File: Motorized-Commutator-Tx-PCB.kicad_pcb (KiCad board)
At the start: 2 copper layers, 100 x 50 mm, 18 parts, among them J1 NRF24L01, J2 Conn_01x10_Female, J3 Conn_01x14_Female, U1 LEFT_STICK, U2 Teensy4.0, U3 LD1117S33TR_SOT223, U4 RIGHT_STICK

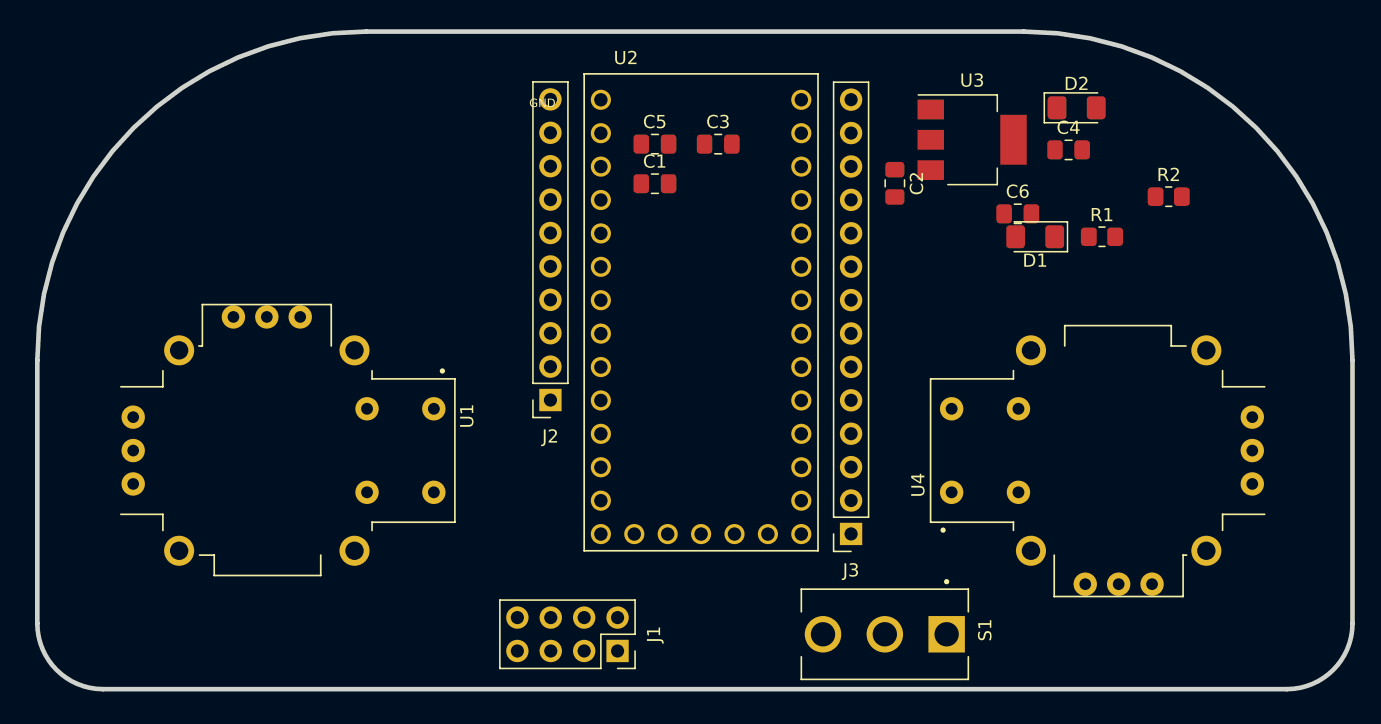
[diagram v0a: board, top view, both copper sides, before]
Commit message: Rewired some connections and completed PCB connections
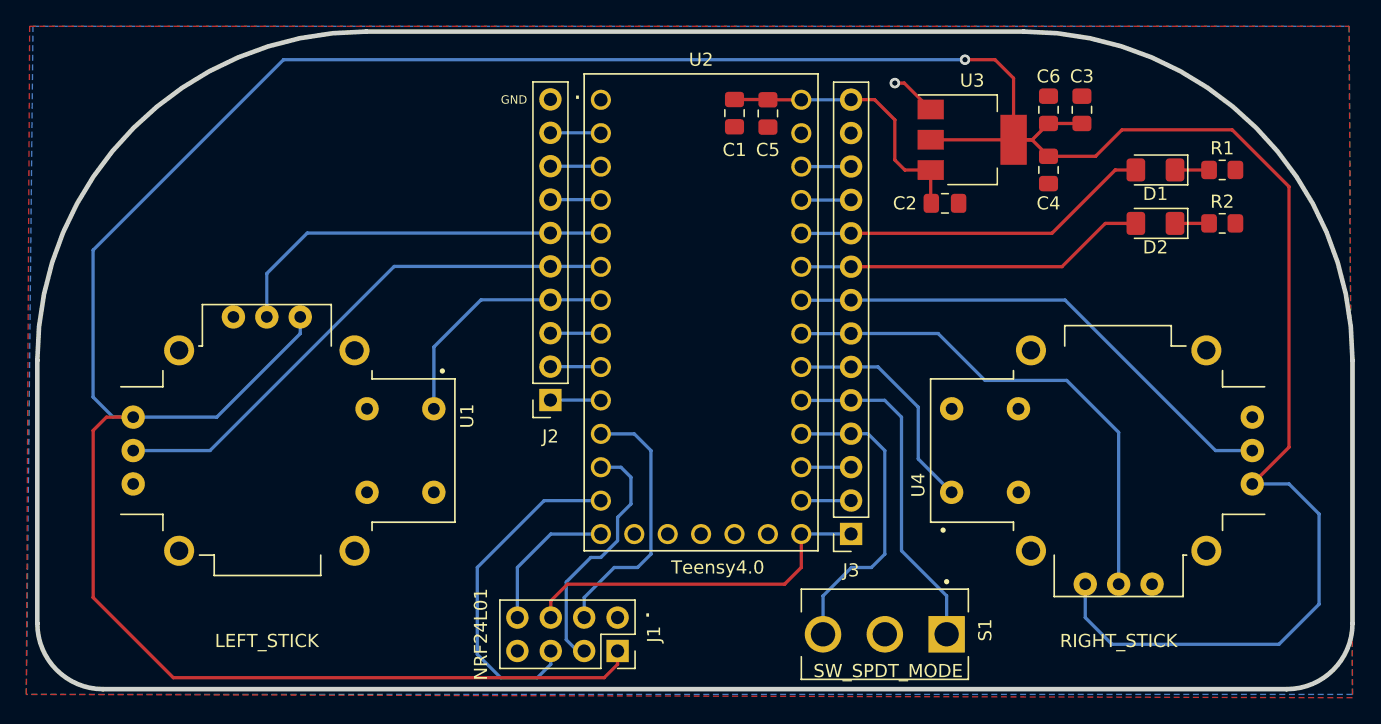
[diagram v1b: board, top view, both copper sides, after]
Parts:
- moved C3 27.8 mm to (156.0, 106.2), turned to 90 degrees
- moved D2 10.6 mm to (161.5, 114.8), turned to 180 degrees
- moved D1 10.5 mm to (161.5, 110.7)
- moved R1 10.5 mm to (166.6, 110.7)
- moved C5 8.90 mm to (132.1, 106.4), turned to -90 degrees
- moved C6 8.25 mm to (153.4, 106.2), turned to 90 degrees
- moved C1 8.09 mm to (129.5, 106.4), turned to -90 degrees
- moved R2 4.54 mm to (166.6, 114.8)
- moved C2 4.10 mm to (145.5, 113.3), turned to 0 degrees
- moved C4 2.16 mm to (153.4, 110.7), turned to -90 degrees
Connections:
- J3 pad 10: Net-(J3-Pad10) -> MANUAL
- J3 pad 2: AUTO -> Net-(J3-Pad2)
- J3 pad 3: MANUAL -> Net-(J3-Pad3)
- J3 pad 6: RIGHT_V -> RIGHT_B
- J3 pad 7: RIGHT_H -> RIGHT_V
- J3 pad 8: RIGHT_B -> RIGHT_H
- J3 pad 9: Net-(J3-Pad9) -> AUTO
- U2 pad 14: AUTO -> Net-(J3-Pad2)
- U2 pad 15: MANUAL -> Net-(J3-Pad3)
- U2 pad 18: RIGHT_V -> RIGHT_B
- U2 pad 19: RIGHT_H -> RIGHT_V
- U2 pad 20: RIGHT_B -> RIGHT_H
- U2 pad 21: Net-(J3-Pad9) -> AUTO
- U2 pad 22: Net-(J3-Pad10) -> MANUAL
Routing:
- net 3.3V: track 0.00 -> 267.9 mm, vias 0 -> 1
- net LEFT_H: track 0.00 -> 41.4 mm
- net RIGHT_H: track 0.00 -> 39.0 mm
- net RIGHT_V: track 0.00 -> 38.8 mm
- net LEFT_V: track 0.00 -> 30.0 mm
- net SCK: track 0.00 -> 27.7 mm
- net MANUAL: track 0.00 -> 27.4 mm
- net AUTO: track 0.00 -> 26.8 mm
- net MANUAL_MODE: track 0.00 -> 26.1 mm
- net MOSI: track 0.00 -> 25.9 mm
- net AUTO_MODE: track 0.00 -> 23.7 mm
- net +5V: track 0.00 -> 21.5 mm
- net CE: track 0.00 -> 20.2 mm
- net CS: track 0.00 -> 19.2 mm
- net LEFT_B: track 0.00 -> 18.9 mm
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- added copper zone on B.Cu, net GND
- added copper zone on F.Cu, net GND
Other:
- board text added: "."
